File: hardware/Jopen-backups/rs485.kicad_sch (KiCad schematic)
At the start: 8 parts, among them U3 SN65HVD1786D

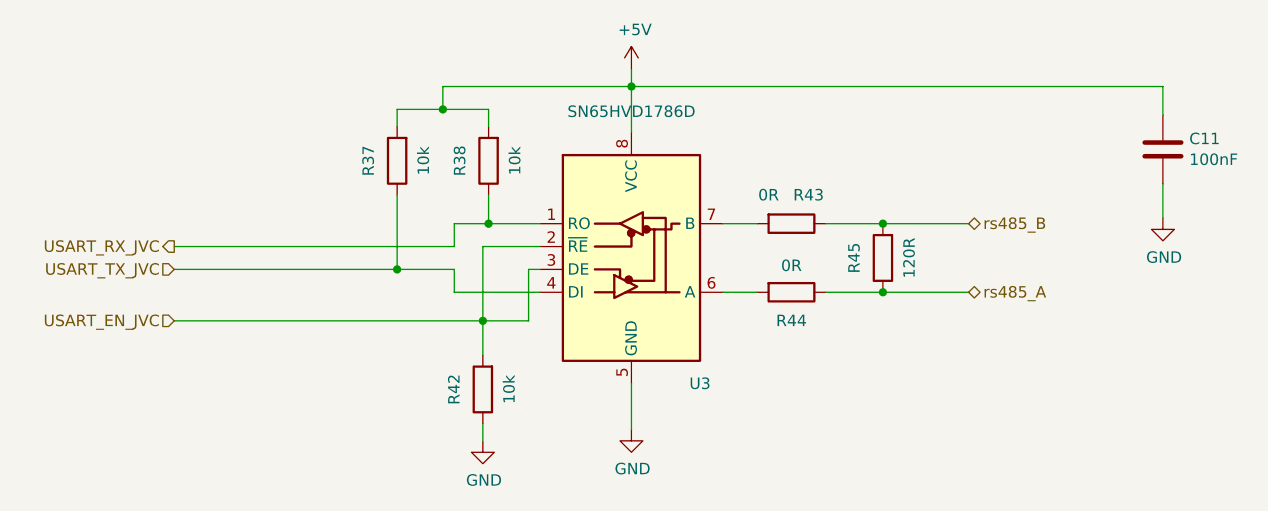
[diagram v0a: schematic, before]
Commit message: Fix P1 IN3 and P2 ADC4 pin configuration
Firmware changes:
- Disabled ADC peripheral initialization (MX_ADC1_Init and HAL_ADC_MspInit)
- Added GPIO pull-up resistors for all button inputs (active-low logic)
- Fixed keyboard HID descriptor (6KRO standard format, 47 bytes)
- Added LED debug indicators (LED1=P1, LED2=P2)
- Device name now conditional based on mode (Keyboard/Joystick/JVS)
- Fixed pin mappings for dual arcade controls (34 inputs total)

Hardware changes:
- Updated KiCad files (v6+ format)
- Added netlist (Jopen.net) for pin verification
- Added flash.ps1 script for automated programming
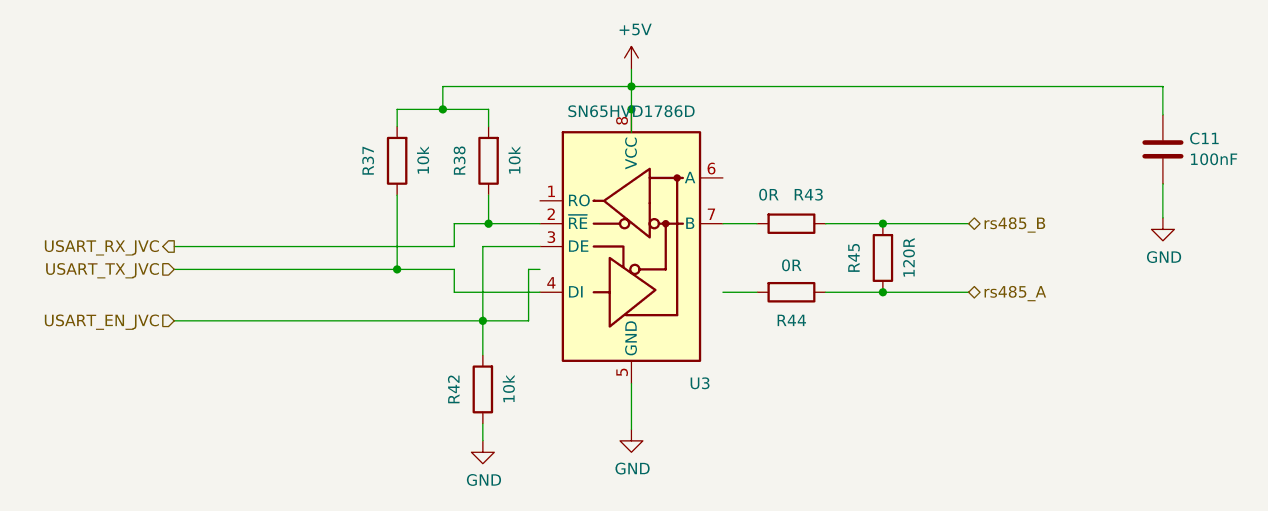
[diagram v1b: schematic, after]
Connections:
- net USART_EN_JVC: no longer U3.2 (~{RE})
- net USART_RX_JVC: now also U3.2 (~{RE}); no longer U3.1 (RO)
- net at U3.6 (A): no longer R44.2
